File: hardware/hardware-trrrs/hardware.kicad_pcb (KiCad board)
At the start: 2 copper layers, 123.4 x 109.1 mm, 81 parts, among them J2 Barrel_Jack, M1 Stepper_Motor_unipolar_5pin, M10 Stepper_Motor_unipolar_5pin, M11 Stepper_Motor_unipolar_5pin, M12 Stepper_Motor_unipolar_5pin, M13 Stepper_Motor_unipolar_5pin, M14 Stepper_Motor_unipolar_5pin, M2 Stepper_Motor_unipolar_5pin, M3 Stepper_Motor_unipolar_5pin, M4 Stepper_Motor_unipolar_5pin, M5 Stepper_Motor_unipolar_5pin, M6 Stepper_Motor_unipolar_5pin, M7 Stepper_Motor_unipolar_5pin, M8 Stepper_Motor_unipolar_5pin, M9 Stepper_Motor_unipolar_5pin, SW1 SW_Push_SPDT, SW10 SW_Push_SPDT, SW11 SW_Push_SPDT, SW12 SW_Push_SPDT, SW13 SW_Push_SPDT, SW14 SW_Push_SPDT, SW15 SW_Push_SPDT, SW16 SW_Push_SPDT, SW2 SW_Push_SPDT, SW3 SW_Push_SPDT, SW4 SW_Push_SPDT, SW5 SW_Push_SPDT, SW6 SW_Push_SPDT, SW7 SW_Push_SPDT, SW8 SW_Push_SPDT, SW9 SW_Push_SPDT, U1 WeMos_D1_mini, U10 ULN2003A, U11 ULN2003A, U12 ULN2003A, U13 ULN2003A, U14 ULN2003A, U15 ULN2003A, U16 ULN2003A, U17 ULN2003A, U2 CD4051B, U3 CD4051B, U4 ULN2003A, U5 ULN2003A, U6 ULN2003A, U7 ULN2003A, U8 ULN2003A, U9 ULN2003A

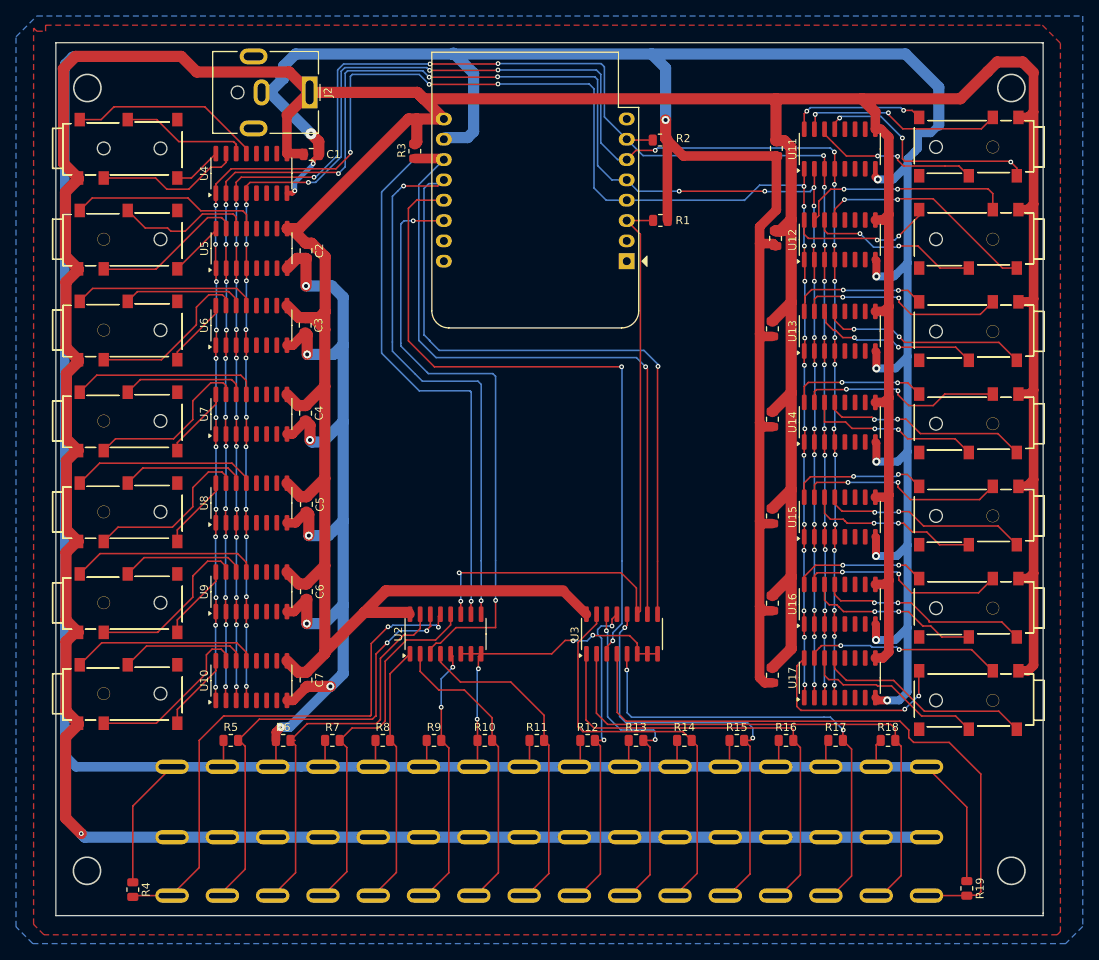
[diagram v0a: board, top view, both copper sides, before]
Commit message: added new pcb revision (trrrs)
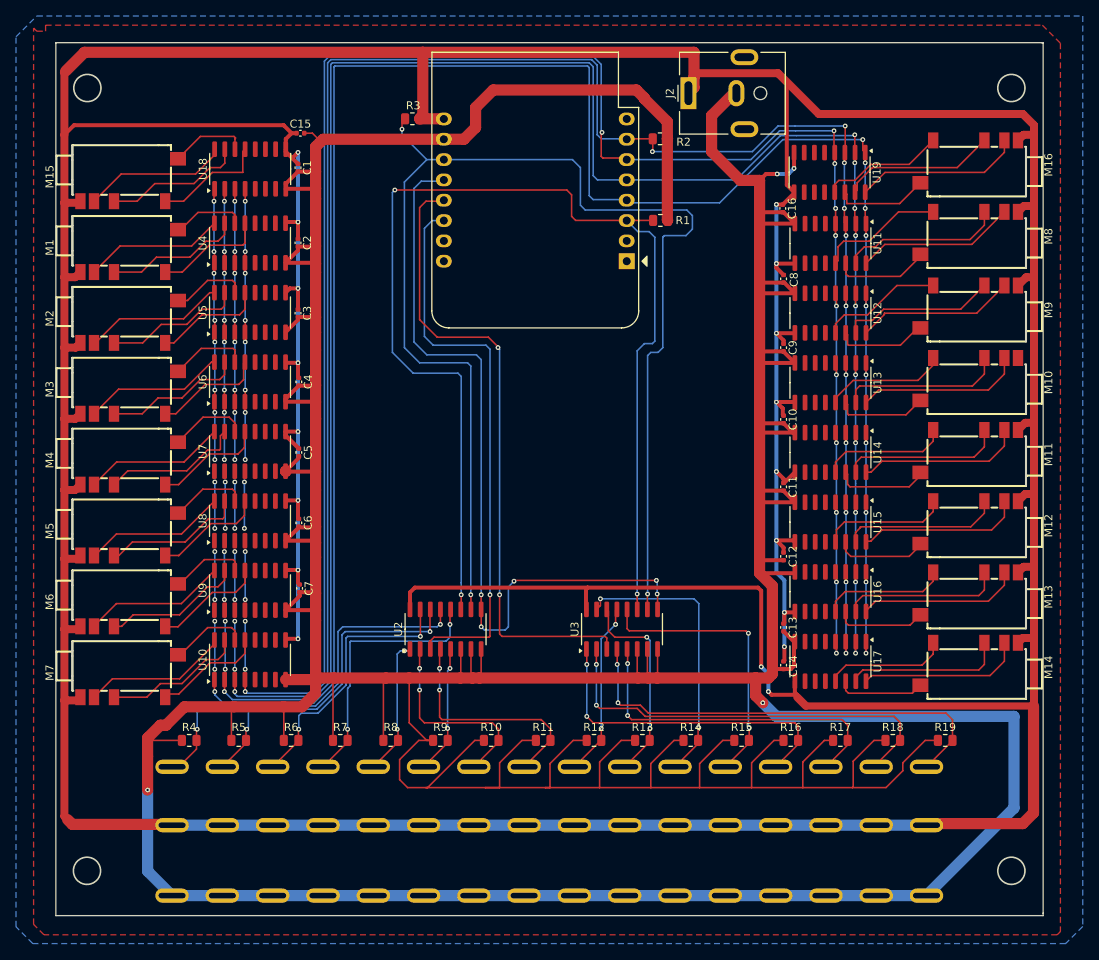
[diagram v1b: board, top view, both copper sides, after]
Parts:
- added C15: 10pF, Capacitor_SMD:C_0402_1005Metric, F.Cu at (188.5, 54.8)
- added C16: 10pF, Capacitor_SMD:C_0402_1005Metric, F.Cu at (248.8, 64.2)
- added M15: Stepper_Motor_unipolar_5pin, Connector_Audio:AUDIO-SMD_STX-3542-5N-G-TR, F.Cu at (167.1, 60.7)
- added M16: Stepper_Motor_unipolar_5pin, Connector_Audio:AUDIO-SMD_STX-3542-5N-G-TR, F.Cu at (272.1, 58.4)
- added U18: ULN2003A, Package_SO:SOIC-16_3.9x9.9mm_P1.27mm, F.Cu at (182.2, 59.3)
- added U19: ULN2003A, Package_SO:SOIC-16_3.9x9.9mm_P1.27mm, F.Cu at (254.7, 59.7)
- C1, C10, C11, C12, C13, C14, C2, C3, C4, C5, C6, C7, C8, C9: footprint Capacitor_SMD:C_0805_2012Metric -> Capacitor_SMD:C_0402_1005Metric
- M1, M10, M11, M12, M13, M14, M2, M3, M4, M5, M6, M7, M8, M9: footprint Connector_Audio:HOOYA-PJ-3505A_C19190915-Jack_3.5mm_PJ31060-I_Horizontal -> Connector_Audio:AUDIO-SMD_STX-3542-5N-G-TR
- moved J2 47.4 mm to (237.0, 49.8), turned to 90 degrees
- moved R4 19.9 mm to (174.6, 130.7), turned to 0 degrees
- moved R19 18.7 mm to (269.1, 130.7), turned to 0 degrees
- moved C8 16.3 mm to (248.9, 73.0)
- moved SW1 16.1 mm to (172.5, 150.1), turned to 90 degrees
- moved SW10 16.1 mm to (229.0, 150.1), turned to 90 degrees
- moved SW11 16.1 mm to (235.3, 150.1), turned to 90 degrees
- moved SW12 16.1 mm to (241.6, 150.1), turned to 90 degrees
- moved SW13 16.1 mm to (247.9, 150.1), turned to 90 degrees
- moved SW14 16.1 mm to (254.2, 150.1), turned to 90 degrees
- moved SW15 16.1 mm to (260.5, 150.1), turned to 90 degrees
- moved SW16 16.1 mm to (266.8, 150.1), turned to 90 degrees
- moved SW2 16.1 mm to (178.7, 150.1), turned to 90 degrees
- moved SW3 16.1 mm to (185.0, 150.1), turned to 90 degrees
- moved SW4 16.1 mm to (191.3, 150.1), turned to 90 degrees
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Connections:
- M1 pad 3: PINK1 -> YELLOW1
- M1 pad 4: YELLOW1 -> PINK1
- M10 pad 3: PINK10 -> YELLOW10
- M10 pad 4: YELLOW10 -> PINK10
- M11 pad 3: PINK11 -> YELLOW11
- M11 pad 4: YELLOW11 -> PINK11
- M12 pad 3: PINK12 -> YELLOW12
- M12 pad 4: YELLOW12 -> PINK12
- M13 pad 3: PINK13 -> YELLOW13
- M13 pad 4: YELLOW13 -> PINK13
- M14 pad 3: PINK14 -> YELLOW14
- M14 pad 4: YELLOW14 -> PINK14
- M2 pad 3: PINK2 -> YELLOW2
- M2 pad 4: YELLOW2 -> PINK2
- M3 pad 3: PINK3 -> YELLOW3
- M3 pad 4: YELLOW3 -> PINK3
- M4 pad 3: PINK4 -> YELLOW4
- M4 pad 4: YELLOW4 -> PINK4
- M5 pad 3: PINK5 -> YELLOW5
- M5 pad 4: YELLOW5 -> PINK5
- M6 pad 3: PINK6 -> YELLOW6
- M6 pad 4: YELLOW6 -> PINK6
- M7 pad 3: PINK7 -> YELLOW7
- M7 pad 4: YELLOW7 -> PINK7
- M8 pad 3: PINK8 -> YELLOW8
- M8 pad 4: YELLOW8 -> PINK8
- M9 pad 3: PINK9 -> YELLOW9
- M9 pad 4: YELLOW9 -> PINK9
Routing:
- net IN1: track 232.0 -> 305.6 mm, vias 28 -> 25
- net IN2: track 230.3 -> 300.2 mm, vias 30 -> 25
- net IN3: track 230.5 -> 294.8 mm, vias 28 -> 26
- net IN4: track 229.4 -> 292.7 mm, vias 29 -> 26
- net A: track 84.9 -> 147.3 mm, vias 2 -> 3
- net C: track 151.6 -> 97.3 mm, vias 3 -> 5
- net SW16: track 78.2 -> 56.7 mm, vias 0 -> 2
- net BLUE16: track 0.00 -> 21.0 mm
- net RED: track 778.0 -> 797.9 mm, vias 1 -> 18
- net SW1: track 68.7 -> 49.2 mm
- net PINK16: track 0.00 -> 19.4 mm
- net SW9: track 40.4 -> 21.9 mm
- net SW12: track 54.1 -> 35.8 mm
- net BLUE15: track 0.00 -> 18.2 mm
- net SW10: track 43.5 -> 25.6 mm
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
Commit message: Updated pcb
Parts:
- moved M1 2.14 mm to (165.0, 69.5)
- moved M2 2.14 mm to (165.0, 78.4)
- moved M3 2.14 mm to (165.0, 87.2)
- moved M4 2.14 mm to (165.0, 96.1)
- moved M5 2.14 mm to (165.0, 104.9)
- moved M7 2.14 mm to (165.0, 122.7)
- moved M15 2.10 mm to (165.0, 60.7)
- moved M6 2.10 mm to (165.0, 113.8)
- moved M10 2.10 mm to (274.2, 85.5)
- moved M11 2.10 mm to (274.2, 94.5)
- moved M12 2.10 mm to (274.2, 103.5)
- moved M13 2.10 mm to (274.2, 112.3)
- moved M14 2.10 mm to (274.2, 121.2)
- moved M16 2.10 mm to (274.2, 58.4)
- moved M8 2.10 mm to (274.2, 67.3)
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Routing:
- net RED: track 797.9 -> 765.2 mm
- net IN2: track 300.2 -> 310.1 mm
- net IN1: track 305.6 -> 315.4 mm
- net IN4: track 292.7 -> 302.5 mm
- net IN3: track 294.8 -> 304.5 mm
- net PINK2: track 17.4 -> 19.7 mm
- net PINK5: track 17.8 -> 20.1 mm
- net PINK6: track 17.4 -> 19.6 mm
- net ORANGE7: track 13.9 -> 16.1 mm
- net BLUE4: track 17.8 -> 19.9 mm
- net BLUE1: track 17.6 -> 19.7 mm
- net PINK1: track 17.2 -> 19.3 mm
- net YELLOW2: track 9.50 -> 11.6 mm
- net YELLOW7: track 9.82 -> 12.0 mm
- net YELLOW5: track 9.65 -> 11.8 mm
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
